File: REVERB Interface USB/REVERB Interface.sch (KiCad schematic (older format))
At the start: 68 parts, among them J1 RPiZeroW, J10 USBPWR, J2 Iridium, J3 APRS, J4 Antenna, J6 USB_B_Micro, J7 USB, J8 USBPOGO, J9 USB SWITCH, M1 MountingHole_Pad, M2 MountingHole_Pad, M3 MountingHole_Pad, M4 MountingHole_Pad, M5 PiMount, M6 PiMount, M7 PiMount, M8 PiMount, U1 IMU, U2 MAX3232, U3 CY7C65213-28PVXI, U4 TXB0104D, U5 DS3232M

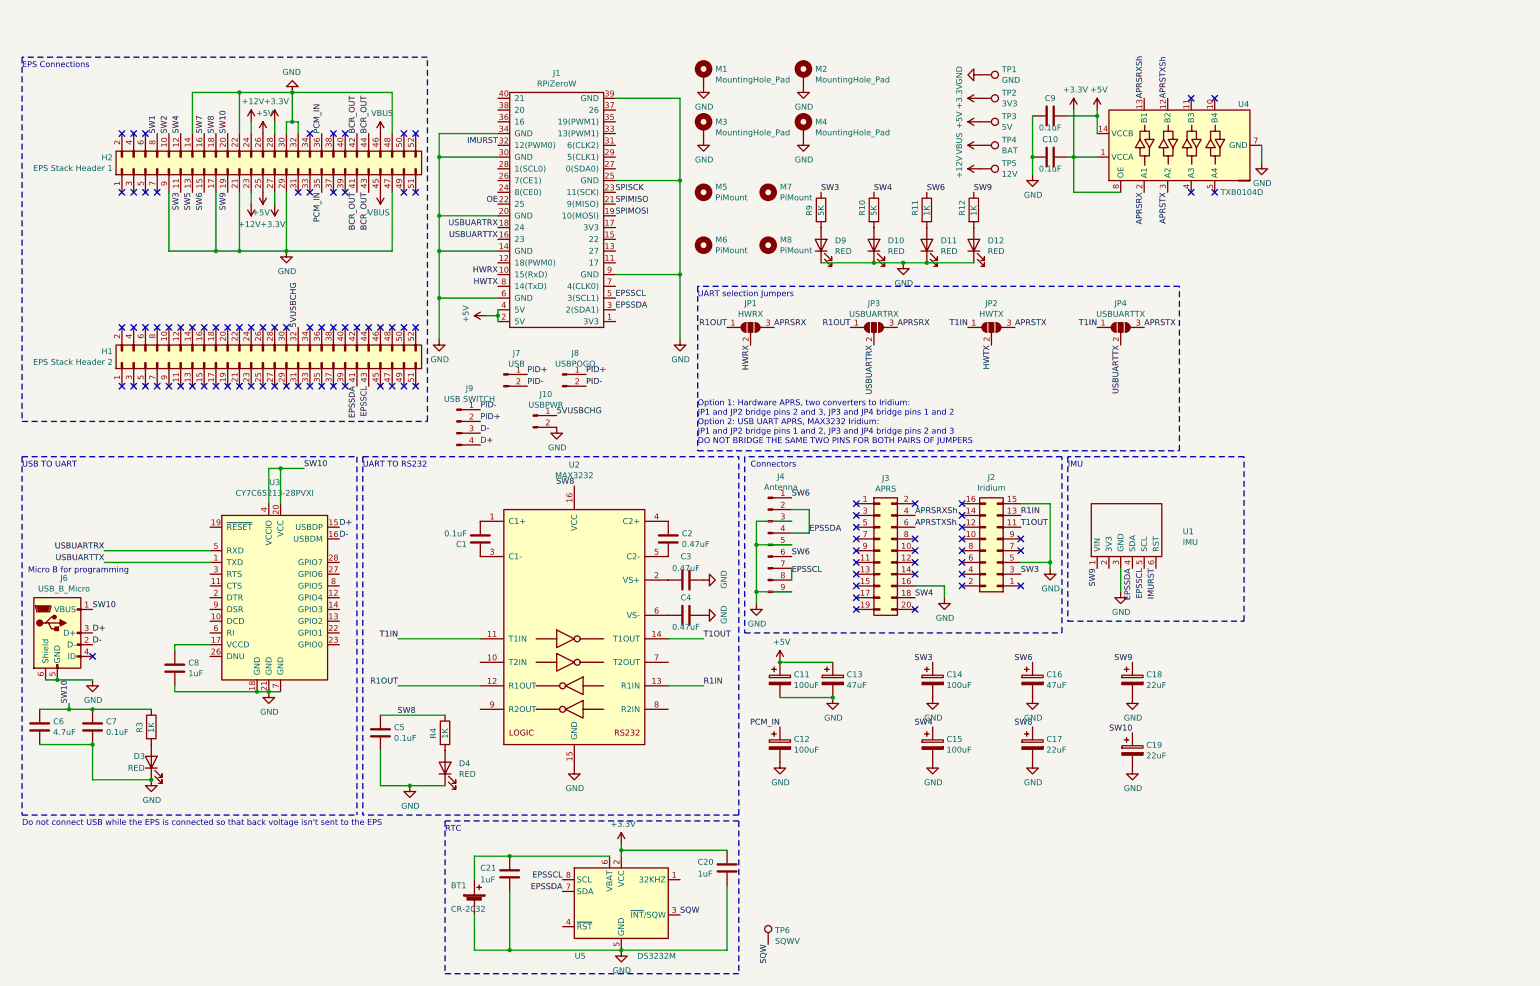
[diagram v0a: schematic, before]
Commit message: start on adding i2c-0 option
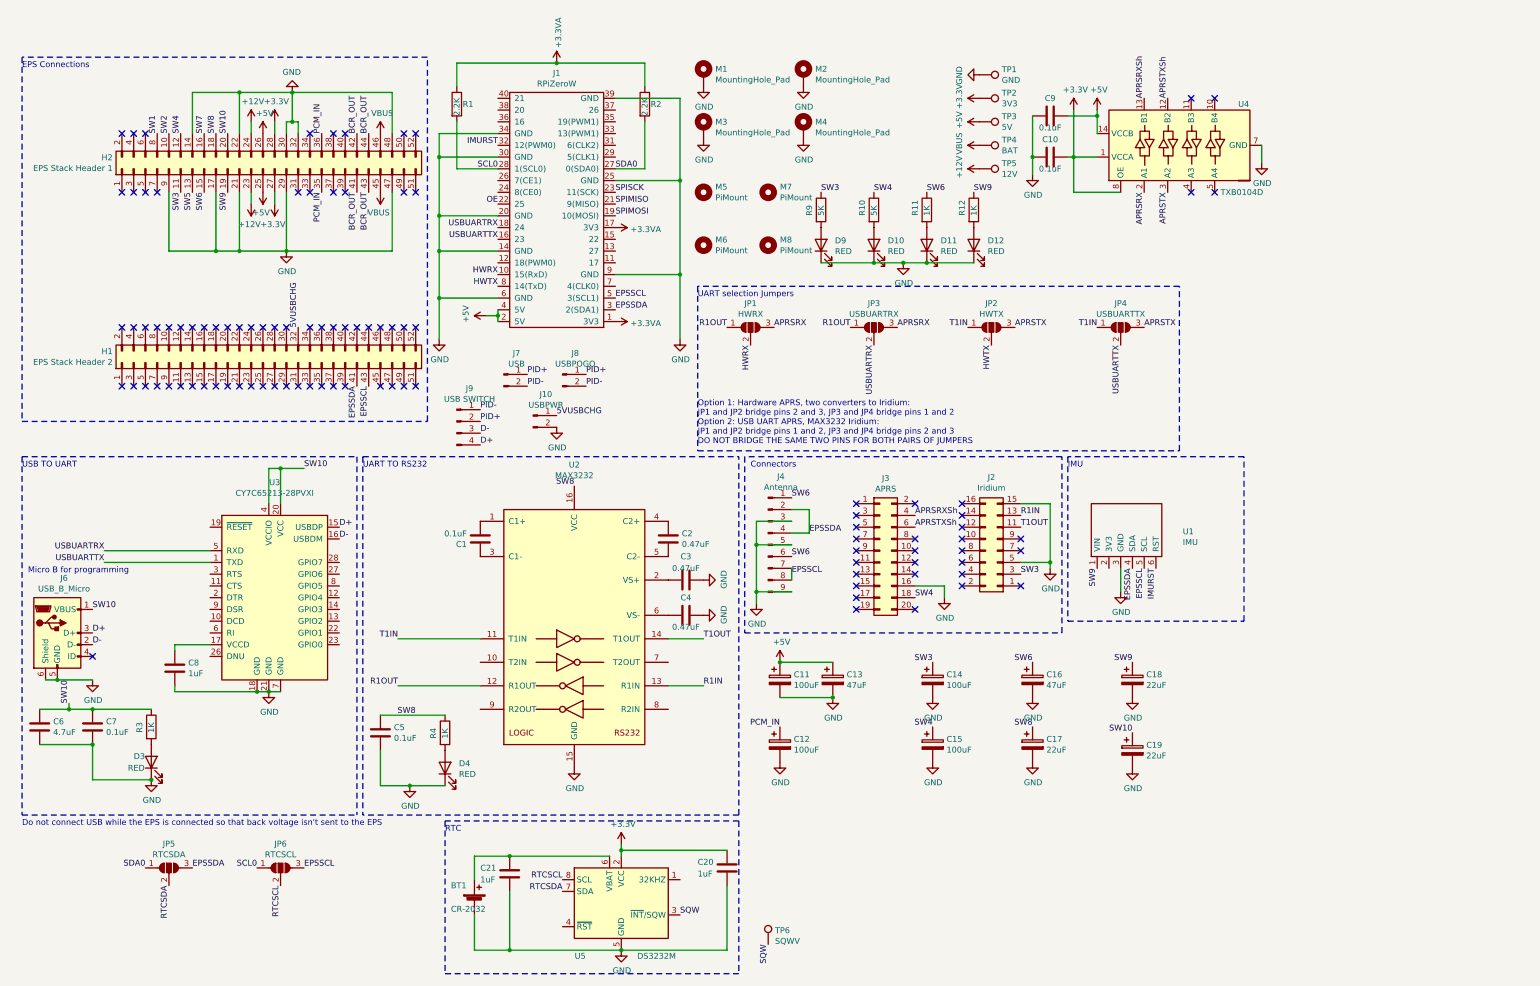
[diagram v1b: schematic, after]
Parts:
- added JP5: RTCSDA, Jumper:SolderJumper-3_P1.3mm_Open_Pad1.0x1.5mm_NumberLabels, symbol Jumper:SolderJumper_3_Open
- added JP6: RTCSCL, Jumper:SolderJumper-3_P1.3mm_Open_Pad1.0x1.5mm_NumberLabels, symbol Jumper:SolderJumper_3_Open
- added R1, R2: 2.2K, Resistor_SMD:R_1206_3216Metric_Pad1.30x1.75mm_HandSolder, symbol Device:R
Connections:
- net EPSSCL: now also JP6.3 (B); no longer U5.8 (SCL)
- net EPSSDA: now also JP5.3 (B); no longer U5.7 (SDA)
- net +3.3VA: now reaches J1.1 (3V3)
- net +3.3VA: now also J1.17 (3V3), R1.1, R2.1
- net SDA0: now reaches J1.27 (0(SDA0))
- net SDA0: now also JP5.1 (A), R2.2
- net SCL0: now reaches J1.28 (1(SCL0))
- net SCL0: now also JP6.1 (A), R1.2
- new net RTCSCL: JP6.2 (C), U5.8 (SCL)
- new net RTCSDA: JP5.2 (C), U5.7 (SDA)
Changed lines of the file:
@@
 	1    0    0    -1
 $EndComp
-Text Label 5100 7500 2    50   ~ 0
-EPSSCL
-Text Label 5100 7600 2    50   ~ 0
-EPSSDA
 $Comp
 L power:GND #PWR014
@@
 Wire Wire Line
 	3700 5850 4400 5850
+Text Label 5550 1450 0    50   ~ 0
+SDA0
+Text Label 4550 1450 2    50   ~ 0
+SCL0
+$Comp
+L power:+3.3VA #PWR016
+U 1 1 61A0DA39
+P 5550 1950
+F 0 "#PWR016" H 5550 1800 50  0001 C CNN
+F 1 "+3.3VA" V 5565 2078 50  0000 L CNN
+F 2 "" H 5550 1950 50  0001 C CNN
+F 3 "" H 5550 1950 50  0001 C CNN
+	1    5550 1950
+	0    1    1    0
+$EndComp
+$Comp
+L power:+3.3VA #PWR017
+U 1 1 61A134B1
+P 5550 2750
+F 0 "#PWR017" H 5550 2600 50  0001 C CNN
+F 1 "+3.3VA" V 5565 2878 50  0000 L CNN
+F 2 "" H 5550 2750 50  0001 C CNN
+F 3 "" H 5550 2750 50  0001 C CNN
+	1    5550 2750
+	0    1    1    0
+$EndComp
+$Comp
+L power:+3.3VA #PWR015
+U 1 1 61A1BE18
+P 5050 550
+F 0 "#PWR015" H 5050 400 50  0001 C CNN
+F 1 "+3.3VA" V 5065 678 50  0000 L CNN
+F 2 "" H 5050 550 50  0001 C CNN
+F 3 "" H 5050 550 50  0001 C CNN
+	1    5050 550
+	1    0    0    -1
+$EndComp
+$Comp
+L Device:R R2
+U 1 1 61A20402
+P 5800 900
+F 0 "R2" H 5850 900 50  0000 L CNN
+F 1 "2.2K" V 5800 800 50  0000 L CNN
+F 2 "Resistor_SMD:R_1206_3216Metric_Pad1.30x1.75mm_HandSolder" V 5730 900 50  0001 C CNN
+F 3 "~" H 5800 900 50  0001 C CNN
+	1    5800 900
+	1    0    0    -1
+$EndComp
+$Comp
+L Device:R R1
+U 1 1 61A20A54
+P 4200 900
+F 0 "R1" H 4250 900 50  0000 L CNN
+F 1 "2.2K" V 4200 800 50  0000 L CNN
+F 2 "Resistor_SMD:R_1206_3216Metric_Pad1.30x1.75mm_HandSolder" V 4130 900 50  0001 C CNN
+F 3 "~" H 4200 900 50  0001 C CNN
+	1    4200 900
+	1    0    0    -1
+$EndComp
+Wire Wire Line
+	5550 1450 5800 1450
+Wire Wire Line
+	5800 1450 5800 1050
+Wire Wire Line
+	4550 1450 4200 1450
+Wire Wire Line
+	4200 1450 4200 1050
+Wire Wire Line
+	4200 750  4200 550
+Wire Wire Line
+	4200 550  5050 550
+Wire Wire Line
+	5050 550  5800 550
+Wire Wire Line
+	5800 550  5800 750
+Connection ~ 5050 550
+Text Label 5100 7500 2    50   ~ 0
+RTCSCL
+Text Label 5100 7600 2    50   ~ 0
+RTCSDA
+$Comp
+L Jumper:SolderJumper_3_Open JP6
+U 1 1 61A57704
+P 2700 7400
+F 0 "JP6" H 2700 7605 50  0000 C CNN
+F 1 "RTCSCL" H 2700 7514 50  0000 C CNN
+F 2 "Jumper:SolderJumper-3_P1.3mm_Open_Pad1.0x1.5mm_NumberLabels" H 2700 7400 50  0001 C CNN
+F 3 "~" H 2700 7400 50  0001 C CNN
+	1    2700 7400
+	1    0    0    -1
+$EndComp
+$Comp
+L Jumper:SolderJumper_3_Open JP5
+U 1 1 61A59919
+P 1750 7400
+F 0 "JP5" H 1750 7605 50  0000 C CNN
+F 1 "RTCSDA" H 1750 7514 50  0000 C CNN
+F 2 "Jumper:SolderJumper-3_P1.3mm_Open_Pad1.0x1.5mm_NumberLabels" H 1750 7400 50  0001 C CNN
+F 3 "~" H 1750 7400 50  0001 C CNN
+	1    1750 7400
+	1    0    0    -1
+$EndComp
+Text Label 2700 7550 3    50   ~ 0
+RTCSCL
+Text Label 1750 7550 3    50   ~ 0
+RTCSDA
+Text Label 2900 7400 0    50   ~ 0
+EPSSCL
+Text Label 1950 7400 0    50   ~ 0
+EPSSDA
+Text Label 1550 7400 2    50   ~ 0
+SDA0
+Text Label 2500 7400 2    50   ~ 0
+SCL0
 $EndSCHEMATC

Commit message: tidy up the schematic, for usb branch
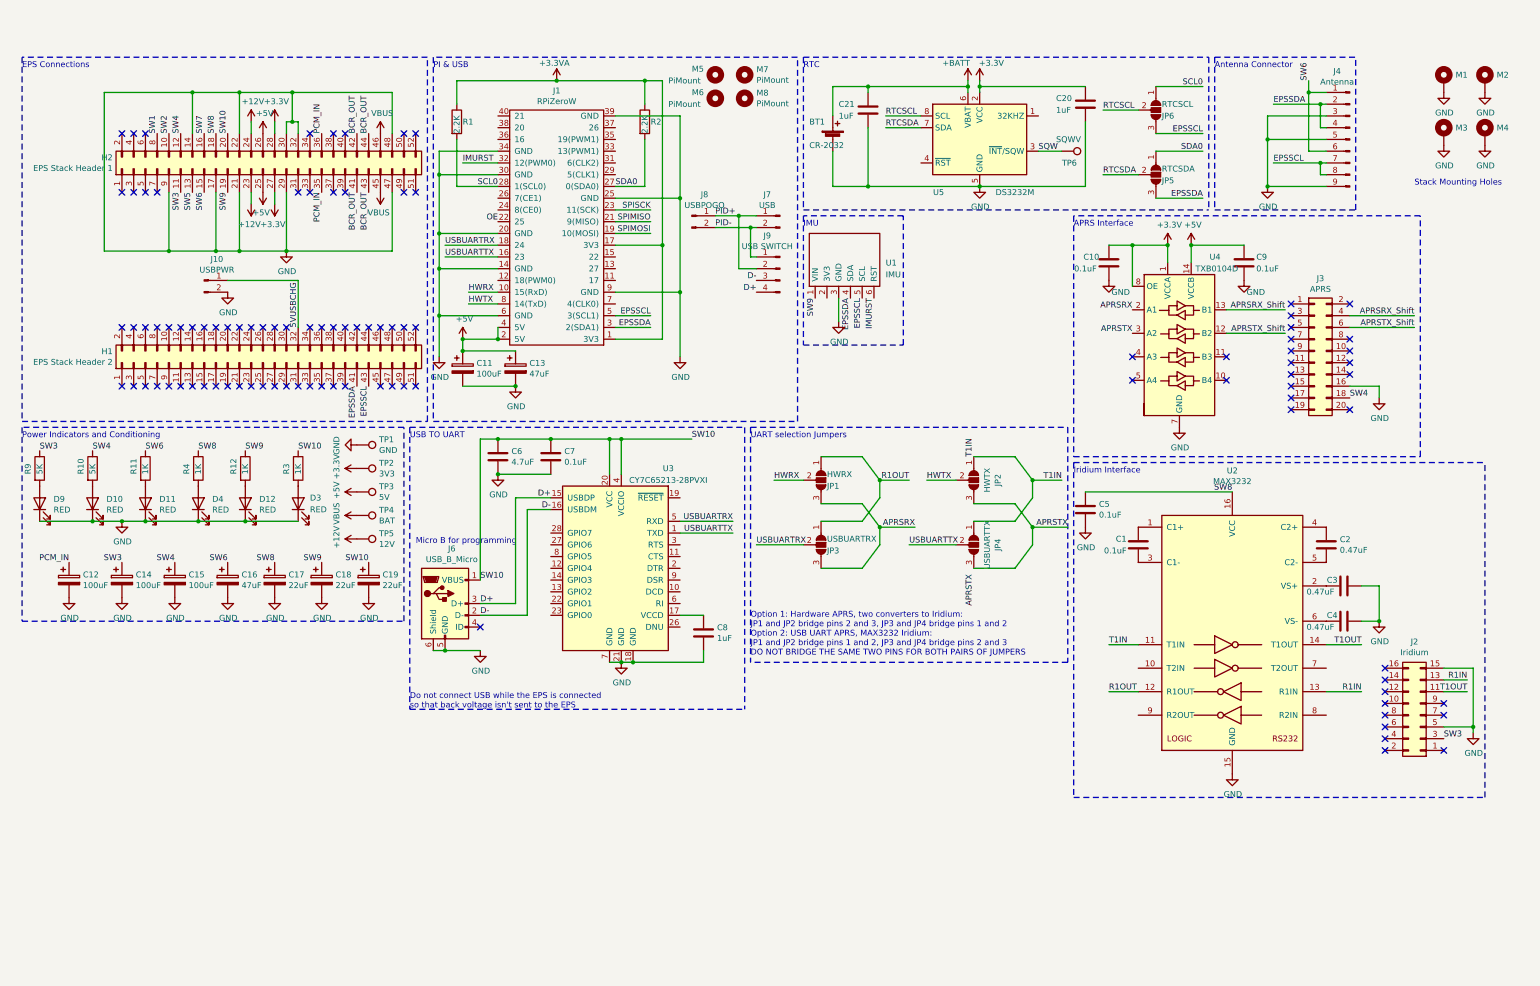
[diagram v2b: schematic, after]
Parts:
- M1, M2, M3, M4: value MountingHole_Pad -> Stack Mounting Hole
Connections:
- net +BATT: now reaches BT1.1 (+), C21.1, U5.6 (VBAT)
- net APRSRXSh renamed APRSRX_Shift
- net APRSTXSh renamed APRSTX_Shift
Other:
- note added: "APRS Interface"
- note added: "Antenna Connector"
- note added: "Do not connect USB while the EPS is connected \nso that back voltage isn't sent to the EPS"
- note added: "Iridium Interface"
- note added: "PI & USB"
- note added: "Power Indicators and Conditioning"
- note added: "Stack Mounting Holes"
- note removed: "Connectors"
- note removed: "Do not connect USB while the EPS is connected so that back voltage isn't sent to the EPS"
- note removed: "UART TO RS232"
- moved on the sheet: BT1, C1, C10, C11, C12, C13, C14, C15, C16, C17, C18, C19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

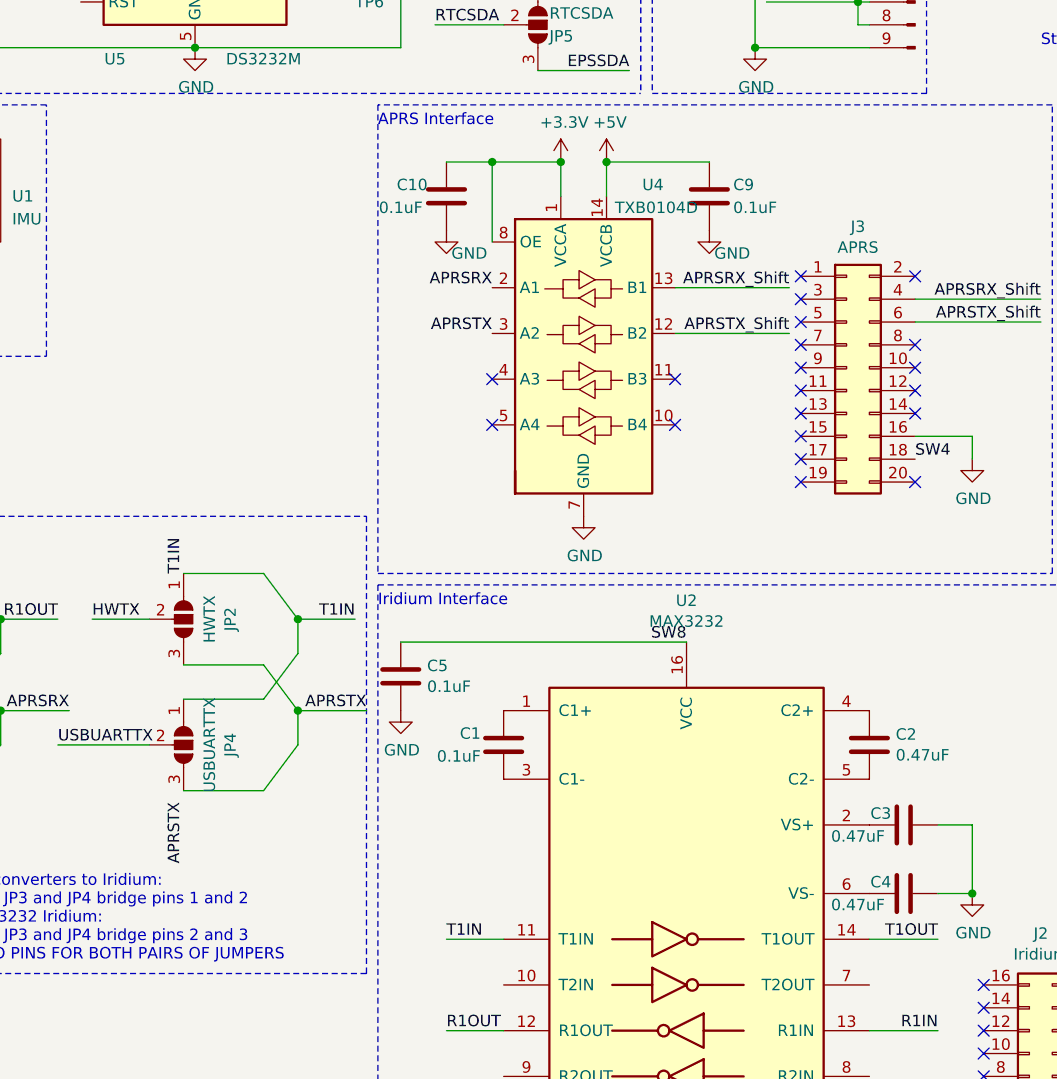
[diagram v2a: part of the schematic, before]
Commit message: finish tidying up schematics
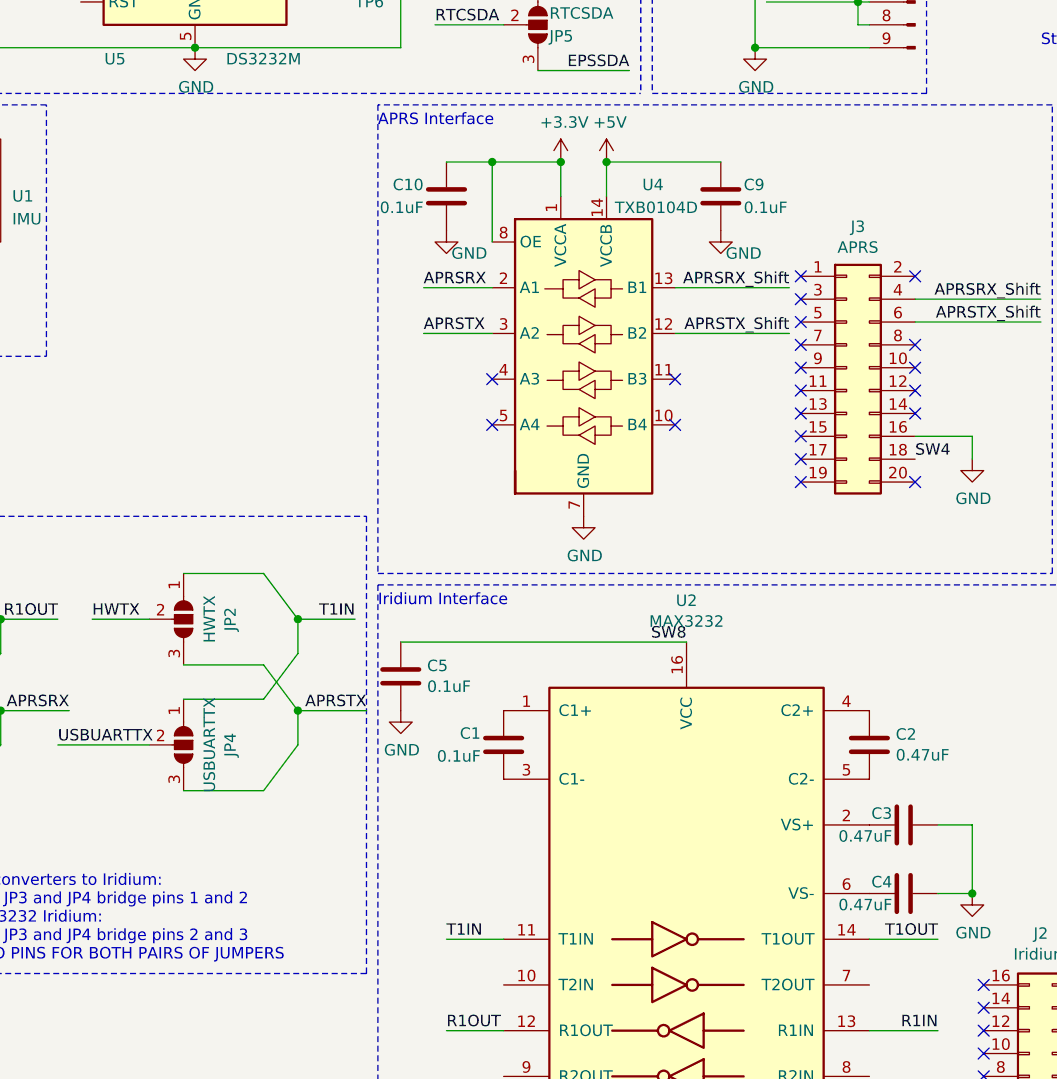
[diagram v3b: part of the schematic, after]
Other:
- moved on the sheet: C9
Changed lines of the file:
@@
 Text Label 8050 4100 2    50   ~ 0
 R1OUT
-Text Label 8600 3900 1    50   ~ 0
-T1IN
 $Comp
 L Device:C C1
@@
 U 1 1 615D2368
 P 11750 5000
-F 0 "C3" V 11700 4900 50  0000 C CNN
-F 1 "0.47uF" V 11800 4800 50  0000 C CNN
+F 0 "C3" V 11700 4950 50  0000 R CNN
+F 1 "0.47uF" V 11800 4950 50  0000 R CNN
 F 2 "Capacitor_SMD:C_0805_2012Metric_Pad1.18x1.45mm_HandSolder" H 11788 4850 50  0001 C CNN
 F 3 "~" H 11750 5000 50  0001 C CNN
@@
 U 1 1 615D50CA
 P 11750 5300
-F 0 "C4" V 11700 5200 50  0000 C CNN
-F 1 "0.47uF" V 11800 5100 50  0000 C CNN
+F 0 "C4" V 11700 5250 50  0000 R CNN
+F 1 "0.47uF" V 11800 5250 50  0000 R CNN
 F 2 "Capacitor_SMD:C_0805_2012Metric_Pad1.18x1.45mm_HandSolder" H 11788 5150 50  0001 C CNN
 F 3 "~" H 11750 5300 50  0001 C CNN
@@
 	0    1    1    0
 $EndComp
-Text Label 8600 4900 3    50   ~ 0
-APRSTX
 Text Label 9350 4100 2    50   ~ 0
 T1IN
@@
 Text Label 11250 2650 2    50   ~ 0
 APRSRX_Shift
-Text Label 9950 2650 2    50   ~ 0
+Text Label 9650 2650 0    50   ~ 0
 APRSRX
-Text Label 9950 2850 2    50   ~ 0
+Text Label 9650 2850 0    50   ~ 0
 APRSTX
 Text Label 4550 1900 2    50   ~ 0
@@
 U 1 1 61853CF1
 P 9750 2250
-F 0 "C10" H 9600 2300 50  0000 C CNN
-F 1 "0.1uF" H 9550 2200 50  0000 C CNN
+F 0 "C10" H 9650 2300 50  0000 R CNN
+F 1 "0.1uF" H 9650 2200 50  0000 R CNN
 F 2 "Capacitor_SMD:C_0805_2012Metric_Pad1.18x1.45mm_HandSolder" H 9788 2100 50  0001 C CNN
 F 3 "~" H 9750 2250 50  0001 C CNN
@@
 L Device:C C9
 U 1 1 618513AF
-P 10900 2250
-F 0 "C9" H 11050 2300 50  0000 C CNN
-F 1 "0.1uF" H 11100 2200 50  0000 C CNN
-F 2 "Capacitor_SMD:C_0805_2012Metric_Pad1.18x1.45mm_HandSolder" H 10938 2100 50  0001 C CNN
-F 3 "~" H 10900 2250 50  0001 C CNN
-	1    10900 2250
-	1    0    0    -1
-$EndComp
-Wire Wire Line
-	10450 2100 10900 2100
+P 10950 2250
+F 0 "C9" H 11050 2300 50  0000 L CNN
+F 1 "0.1uF" H 11050 2200 50  0000 L CNN
+F 2 "Capacitor_SMD:C_0805_2012Metric_Pad1.18x1.45mm_HandSolder" H 10988 2100 50  0001 C CNN
+F 3 "~" H 10950 2250 50  0001 C CNN
+	1    10950 2250
+	1    0    0    -1
+$EndComp
 $Comp
 L power:GND #PWR0101
 U 1 1 61F1DE0F
-P 10900 2400
-F 0 "#PWR0101" H 10900 2150 50  0001 C CNN
-F 1 "GND" H 11000 2300 50  0000 C CNN
-F 2 "" H 10900 2400 50  0001 C CNN
-F 3 "" H 10900 2400 50  0001 C CNN
-	1    10900 2400
+P 10950 2400
+F 0 "#PWR0101" H 10950 2150 50  0001 C CNN
+F 1 "GND" H 11050 2300 50  0000 C CNN
+F 2 "" H 10950 2400 50  0001 C CNN
+F 3 "" H 10950 2400 50  0001 C CNN
+	1    10950 2400
 	1    0    0    -1
 $EndComp
@@
 Text Notes 12350 1600 0    50   ~ 0
 Stack Mounting Holes
+Wire Wire Line
+	10450 2100 10950 2100
+Wire Wire Line
+	9650 2650 9950 2650
+Wire Wire Line
+	9650 2850 9950 2850
 $EndSCHEMATC

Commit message: new gerber exports
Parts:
- C13, C16: value 47uF -> 22uF
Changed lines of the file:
@@
 P 4700 3150
 F 0 "C13" H 4818 3196 50  0000 L CNN
-F 1 "47uF" H 4818 3105 50  0000 L CNN
+F 1 "22uF" H 4818 3105 50  0000 L CNN
 F 2 "Capacitor_Tantalum_SMD:CP_EIA-6032-28_Kemet-C_Pad2.25x2.35mm_HandSolder" H 4738 3000 50  0001 C CNN
 F 3 "~" H 4700 3150 50  0001 C CNN
@@
 P 2250 4950
 F 0 "C16" H 2368 4996 50  0000 L CNN
-F 1 "47uF" H 2368 4905 50  0000 L CNN
+F 1 "22uF" H 2368 4905 50  0000 L CNN
 F 2 "Capacitor_Tantalum_SMD:CP_EIA-6032-28_Kemet-C_Pad2.25x2.35mm_HandSolder" H 2288 4800 50  0001 C CNN
 F 3 "~" H 2250 4950 50  0001 C CNN

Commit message: stack conflict checking
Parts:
- J9: footprint Connector_JST:JST_XH_B4B-XH-A_1x04_P2.50mm_Vertical -> Connector_Molex:Molex_PicoBlade_53047-0410_1x04_P1.25mm_Vertical
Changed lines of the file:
@@
 F 0 "J9" H 7058 2581 50  0000 C CNN
 F 1 "USB SWITCH" H 7058 2490 50  0000 C CNN
-F 2 "Connector_JST:JST_XH_B4B-XH-A_1x04_P2.50mm_Vertical" H 6950 2300 50  0001 C CNN
+F 2 "Connector_Molex:Molex_PicoBlade_53047-0410_1x04_P1.25mm_Vertical" H 6950 2300 50  0001 C CNN
 F 3 "~" H 6950 2300 50  0001 C CNN
 	1    6950 2300
